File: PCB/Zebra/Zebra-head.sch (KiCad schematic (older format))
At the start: 4 parts, among them J1 Conn_01x11, J2 Conn_01x11, U1 ProMicro, U2 ssd1306

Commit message: Switch to foostan's footprint library, MIT license
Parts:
- removed U1: ProMicro, promicro:ProMicro-DualFootprint, symbol promicro:ProMicro
- added U1: ProMicro, kbd:ProMicro_v3.5, symbol kbd:ProMicro
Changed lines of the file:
@@
 Wire Wire Line
 	1750 3100 1450 3100
-$Comp
-L promicro:ProMicro U1
-U 1 1 5FCC9219
-P 2450 3250
-F 0 "U1" H 2450 4393 60  0000 C CNN
-F 1 "ProMicro" H 2450 4287 60  0000 C CNN
-F 2 "promicro:ProMicro-DualFootprint" H 2450 4181 60  0000 C CNN
-F 3 "" H 2550 2200 60  0000 C CNN
-	1    2450 3250
-	1    0    0    -1
-$EndComp
 Wire Wire Line
 	1650 2100 3800 2100
@@
 Wire Wire Line
 	950  2900 950  4950
+$Comp
+L kbd:ProMicro U1
+U 1 1 5FD08ED3
+P 2450 3050
+F 0 "U1" H 2450 3887 60  0000 C CNN
+F 1 "ProMicro" H 2450 3781 60  0000 C CNN
+F 2 "kbd:ProMicro_v3.5" H 2550 2000 60  0000 C CNN
+F 3 "" H 2550 2000 60  0000 C CNN
+	1    2450 3050
+	1    0    0    -1
+$EndComp
 $EndSCHEMATC

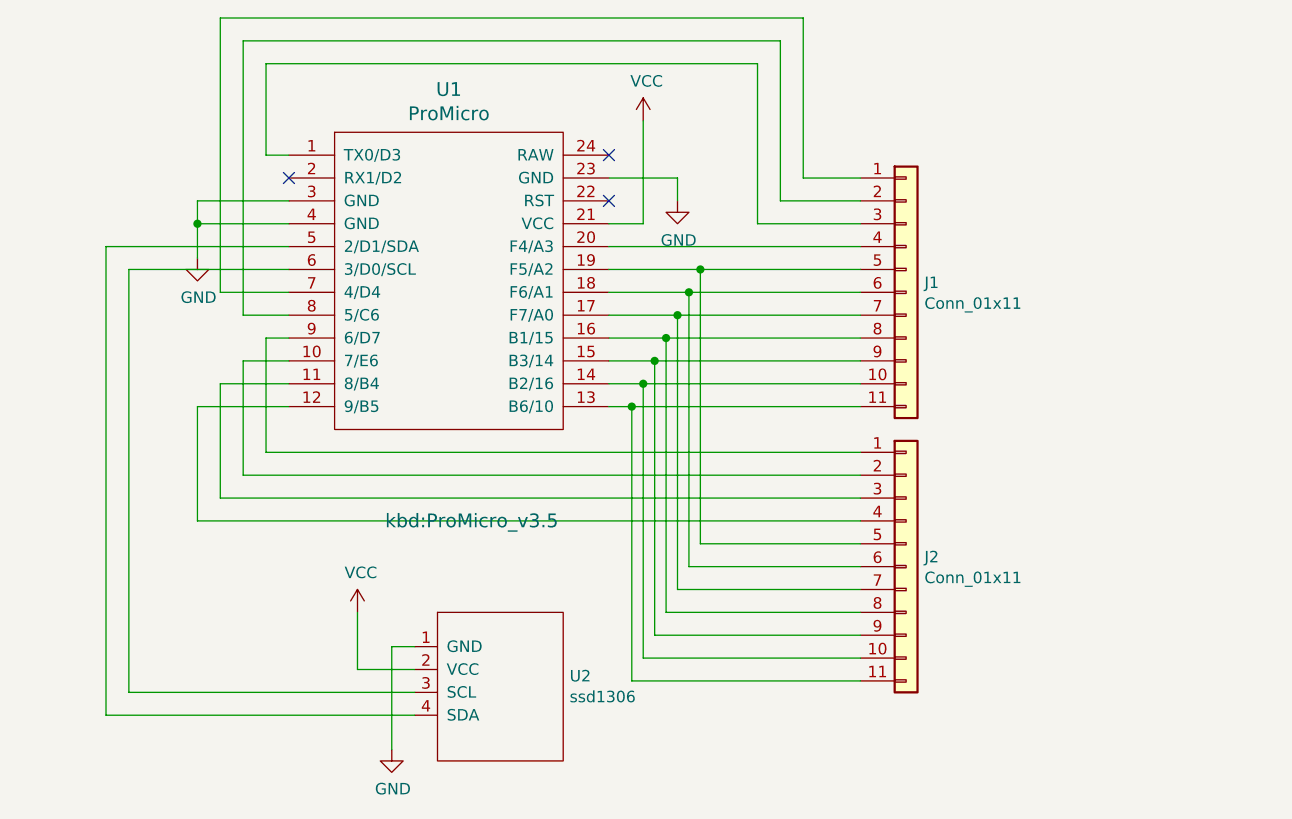
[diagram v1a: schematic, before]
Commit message: Add TRRS jack
With serial and optional I2C
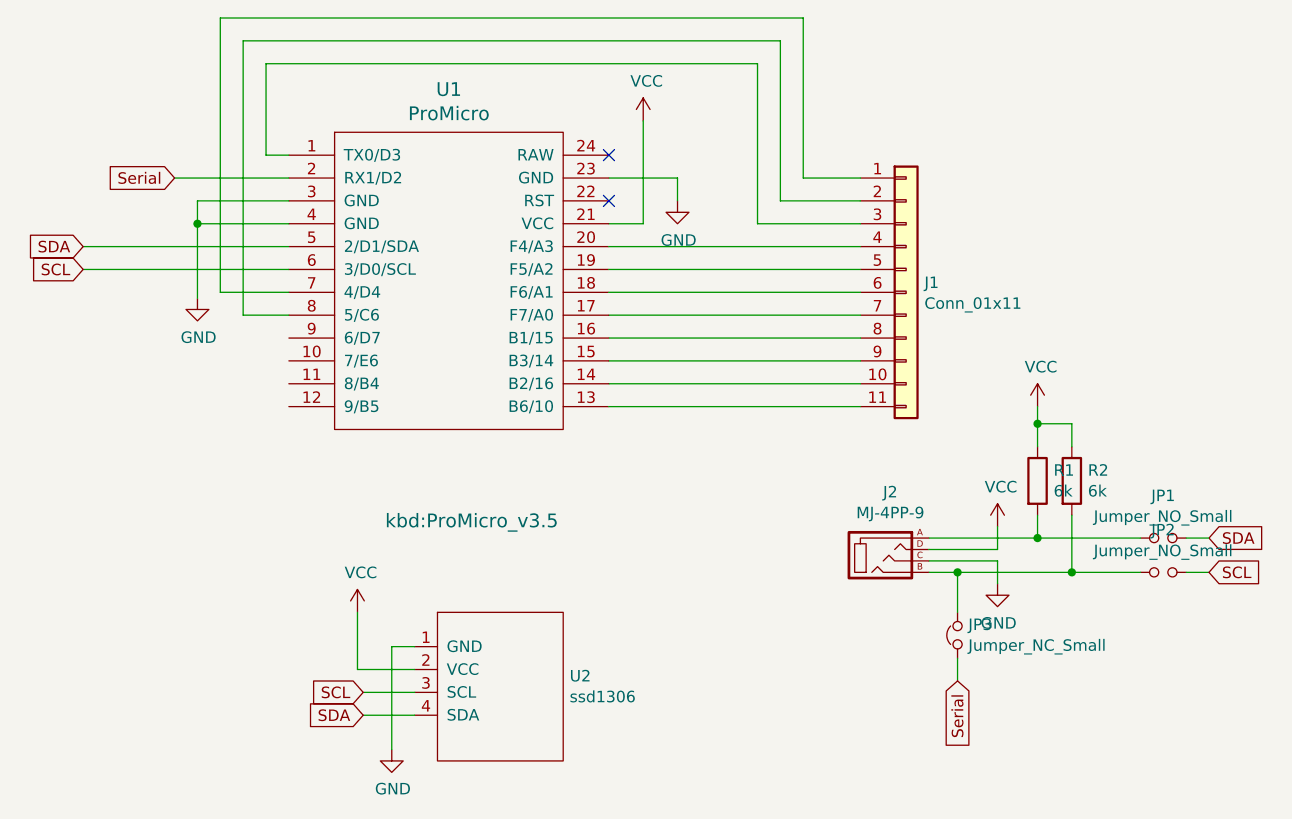
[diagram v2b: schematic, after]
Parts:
- removed J2: Conn_01x11, Connector_PinHeader_2.54mm:PinHeader_1x11_P2.54mm_Vertical, symbol Connector_Generic:Conn_01x11
- added J2: MJ-4PP-9, kbd:MJ-4PP-9_1side, symbol kbd:MJ-4PP-9
- added JP1, JP2: Jumper_NO_Small, Jumper:SolderJumper-2_P1.3mm_Open_Pad1.0x1.5mm, symbol Device:Jumper_NO_Small
- added JP3: Jumper_NC_Small, Jumper:SolderJumper-2_P1.3mm_Bridged_Pad1.0x1.5mm, symbol Device:Jumper_NC_Small
- added R1, R2: 6k, Resistor_SMD:R_1206_3216Metric_Pad1.30x1.75mm_HandSolder, symbol Device:R
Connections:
- net GND: now also J2.C
- net VCC: now also J2.D, R1.1, R2.1
- net SCL: now reaches U1.6 (3/D0/SCL), U2.3 (SCL)
- net SCL: now also JP2.2
- net SDA: now reaches U1.5 (2/D1/SDA), U2.4 (SDA)
- net SDA: now also JP1.2
- net Serial: now reaches U1.2 (RX1/D2)
- net Serial: now also JP3.1
- new net: J2.A, JP1.1, R1.2
- new net: J2.B, JP2.1, JP3.2, R2.2
- no-connect marks 3 -> 2
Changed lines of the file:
@@
 	1    0    0    -1
 $EndComp
-$Comp
-L Connector_Generic:Conn_01x11 J2
-U 1 1 5FA81425
-P 4450 4300
-F 0 "J2" H 4530 4342 50  0000 L CNN
-F 1 "Conn_01x11" H 4530 4251 50  0000 L CNN
-F 2 "Connector_PinHeader_2.54mm:PinHeader_1x11_P2.54mm_Vertical" H 4450 4300 50  0001 C CNN
-F 3 "~" H 4450 4300 50  0001 C CNN
-	1    4450 4300
-	1    0    0    -1
-$EndComp
-Wire Wire Line
-	4250 3600 3250 3600
-Wire Wire Line
-	3150 3500 3300 3500
-Wire Wire Line
-	4250 3400 3350 3400
-Wire Wire Line
-	3150 3300 3400 3300
-Wire Wire Line
-	4250 3200 3450 3200
-Wire Wire Line
-	3150 3100 3500 3100
-Wire Wire Line
-	4250 3000 3550 3000
-Wire Wire Line
-	3250 3600 3250 4800
-Wire Wire Line
-	3250 4800 4250 4800
-Connection ~ 3250 3600
-Wire Wire Line
-	3250 3600 3150 3600
-Wire Wire Line
-	3300 3500 3300 4700
-Wire Wire Line
-	3300 4700 4250 4700
-Connection ~ 3300 3500
-Wire Wire Line
-	3300 3500 4250 3500
-Wire Wire Line
-	3350 3400 3350 4600
-Wire Wire Line
-	3350 4600 4250 4600
-Connection ~ 3350 3400
-Wire Wire Line
-	3350 3400 3150 3400
-Wire Wire Line
-	3400 3300 3400 4500
-Wire Wire Line
-	3400 4500 4250 4500
-Connection ~ 3400 3300
-Wire Wire Line
-	3400 3300 4250 3300
-Wire Wire Line
-	3450 3200 3450 4400
-Wire Wire Line
-	3450 4400 4250 4400
-Connection ~ 3450 3200
-Wire Wire Line
-	3450 3200 3150 3200
-Wire Wire Line
-	3500 3100 3500 4300
-Wire Wire Line
-	3500 4300 4250 4300
-Connection ~ 3500 3100
-Wire Wire Line
-	3500 3100 4250 3100
-Wire Wire Line
-	3550 3000 3550 4200
-Wire Wire Line
-	3550 4200 4250 4200
-Connection ~ 3550 3000
-Wire Wire Line
-	3550 3000 3150 3000
 Wire Wire Line
 	3150 2900 4250 2900
 Wire Wire Line
-	1650 3800 4250 3800
-Wire Wire Line
-	1550 3900 4250 3900
-Wire Wire Line
-	1450 4000 4250 4000
-Wire Wire Line
-	1350 4100 4250 4100
-Wire Wire Line
 	1750 2500 1650 2500
 Wire Wire Line
@@
 Wire Wire Line
 	1750 2800 1350 2800
-Wire Wire Line
-	1350 2800 1350 2950
 $Comp
 L power:GND #PWR01
 U 1 1 5FAB7882
-P 1350 2950
-F 0 "#PWR01" H 1350 2700 50  0001 C CNN
-F 1 "GND" H 1355 2777 50  0000 C CNN
-F 2 "" H 1350 2950 50  0001 C CNN
-F 3 "" H 1350 2950 50  0001 C CNN
-	1    1350 2950
+P 1350 3125
+F 0 "#PWR01" H 1350 2875 50  0001 C CNN
+F 1 "GND" H 1355 2952 50  0000 C CNN
+F 2 "" H 1350 3125 50  0001 C CNN
+F 3 "" H 1350 3125 50  0001 C CNN
+	1    1350 3125
 	1    0    0    -1
 $EndComp
@@
 Wire Wire Line
 	3300 2800 3300 2350
-Wire Wire Line
-	1750 3000 1050 3000
-Wire Wire Line
-	1050 4850 2300 4850
-Wire Wire Line
-	1750 2900 950  2900
-Wire Wire Line
-	950  4950 2300 4950
 $Comp
 L power:GND #PWR03
@@
 NoConn ~ 3150 2500
 NoConn ~ 3150 2700
-NoConn ~ 1750 2600
-Wire Wire Line
-	1650 3300 1750 3300
-Wire Wire Line
-	1650 3300 1650 3800
-Wire Wire Line
-	1450 3500 1750 3500
-Wire Wire Line
-	1450 3500 1450 4000
-Wire Wire Line
-	1550 3400 1750 3400
-Wire Wire Line
-	1550 3400 1550 3900
-Wire Wire Line
-	1750 3600 1350 3600
-Wire Wire Line
-	1350 3600 1350 4100
 Wire Wire Line
 	1550 3200 1750 3200
@@
 	1650 2100 3800 2100
 Wire Wire Line
-	1050 3000 1050 4850
-Wire Wire Line
-	950  2900 950  4950
+	3150 3100 4250 3100
+Wire Wire Line
+	3150 3000 4250 3000
+Wire Wire Line
+	3150 3600 4250 3600
+Wire Wire Line
+	3150 3500 4250 3500
+Wire Wire Line
+	3150 3400 4250 3400
+Wire Wire Line
+	3150 3300 4250 3300
+Wire Wire Line
+	3150 3200 4250 3200
 $Comp
 L kbd:ProMicro U1
@@
 	1    0    0    -1
 $EndComp
+Text GLabel 1250 2600 0    50   Input ~ 0
+Serial
+Wire Wire Line
+	1750 2600 1250 2600
+$Comp
+L kbd:MJ-4PP-9 J2
+U 1 1 5FD0D110
+P 4350 4250
+F 0 "J2" H 4381 4526 50  0000 C CNN
+F 1 "MJ-4PP-9" H 4381 4435 50  0000 C CNN
+F 2 "kbd:MJ-4PP-9_1side" H 4625 4425 50  0001 C CNN
+F 3 "~" H 4625 4425 50  0001 C CNN
+	1    4350 4250
+	1    0    0    -1
+$EndComp
+$Comp
+L power:VCC #PWR0101
+U 1 1 5FD0DF7B
+P 4850 4125
+F 0 "#PWR0101" H 4850 3975 50  0001 C CNN
+F 1 "VCC" H 4865 4298 50  0000 C CNN
+F 2 "" H 4850 4125 50  0001 C CNN
+F 3 "" H 4850 4125 50  0001 C CNN
+	1    4850 4125
+	1    0    0    -1
+$EndComp
+Wire Wire Line
+	4550 4225 4850 4225
+$Comp
+L power:GND #PWR0102
+U 1 1 5FD10450
+P 4850 4375
+F 0 "#PWR0102" H 4850 4125 50  0001 C CNN
+F 1 "GND" H 4855 4202 50  0000 C CNN
+F 2 "" H 4850 4375 50  0001 C CNN
+F 3 "" H 4850 4375 50  0001 C CNN
+	1    4850 4375
+	1    0    0    -1
+$EndComp
+Wire Wire Line
+	4550 4275 4850 4275
+Text GLabel 4675 4800 3    50   Input ~ 0
+Serial
+Wire Wire Line
+	4550 4325 4675 4325
+$Comp
+L Device:Jumper_NO_Small JP1
+U 1 1 5FD0D318
+P 5575 4175
+F 0 "JP1" H 5575 4360 50  0000 C CNN
+F 1 "Jumper_NO_Small" H 5575 4269 50  0000 C CNN
+F 2 "Jumper:SolderJumper-2_P1.3mm_Open_Pad1.0x1.5mm" H 5575 4175 50  0001 C CNN
+F 3 "~" H 5575 4175 50  0001 C CNN
+	1    5575 4175
+	1    0    0    -1
+$EndComp
+$Comp
+L Device:Jumper_NO_Small JP2
+U 1 1 5FD0E0A1
+P 5575 4325
+F 0 "JP2" H 5575 4510 50  0000 C CNN
+F 1 "Jumper_NO_Small" H 5575 4419 50  0000 C CNN
+F 2 "Jumper:SolderJumper-2_P1.3mm_Open_Pad1.0x1.5mm" H 5575 4325 50  0001 C CNN
+F 3 "~" H 5575 4325 50  0001 C CNN
+	1    5575 4325
+	1    0    0    -1
+$EndComp
+Wire Wire Line
+	4850 4125 4850 4225
+Wire Wire Line
+	4850 4275 4850 4375
+Text GLabel 850  2900 0    50   Input ~ 0
+SDA
+Text GLabel 850  3000 0    50   Input ~ 0
+SCL
+Wire Wire Line
+	1750 2900 850  2900
+Wire Wire Line
+	1750 3000 850  3000
+Wire Wire Line
+	1350 2800 1350 3125
+Text GLabel 2075 4950 0    50   Input ~ 0
+SDA
+Text GLabel 2075 4850 0    50   Input ~ 0
+SCL
+Wire Wire Line
+	2300 4850 2075 4850
+Wire Wire Line
+	2300 4950 2075 4950
+Text GLabel 5775 4325 2    50   Input ~ 0
+SCL
+Text GLabel 5775 4175 2    50   Input ~ 0
+SDA
+$Comp
+L power:VCC #PWR0103
+U 1 1 5FD1F947
+P 5025 3600
+F 0 "#PWR0103" H 5025 3450 50  0001 C CNN
+F 1 "VCC" H 5040 3773 50  0000 C CNN
+F 2 "" H 5025 3600 50  0001 C CNN
+F 3 "" H 5025 3600 50  0001 C CNN
+	1    5025 3600
+	1    0    0    -1
+$EndComp
+$Comp
+L Device:R R1
+U 1 1 5FD1FE92
+P 5025 3925
+F 0 "R1" H 5095 3971 50  0000 L CNN
+F 1 "6k" H 5095 3880 50  0000 L CNN
+F 2 "Resistor_SMD:R_1206_3216Metric_Pad1.30x1.75mm_HandSolder" V 4955 3925 50  0001 C CNN
+F 3 "~" H 5025 3925 50  0001 C CNN
+	1    5025 3925
+	1    0    0    -1
+$EndComp
+$Comp
+L Device:R R2
+U 1 1 5FD2335A
+P 5175 3925
+F 0 "R2" H 5245 3971 50  0000 L CNN
+F 1 "6k" H 5245 3880 50  0000 L CNN
+F 2 "Resistor_SMD:R_1206_3216Metric_Pad1.30x1.75mm_HandSolder" V 5105 3925 50  0001 C CNN
+F 3 "~" H 5175 3925 50  0001 C CNN
+	1    5175 3925
+	1    0    0    -1
+$EndComp
+Wire Wire Line
+	5025 3775 5025 3675
+Wire Wire Line
+	5175 3775 5175 3675
+Wire Wire Line
+	5175 3675 5025 3675
+Connection ~ 5025 3675
+Wire Wire Line
+	5025 3675 5025 3600
+$Comp
+L Device:Jumper_NC_Small JP3
+U 1 1 5FD2C94B
+P 4675 4600
+F 0 "JP3" V 4721 4553 50  0000 R CNN
+F 1 "Jumper_NC_Small" V 4630 4553 50  0000 R CNN
+F 2 "Jumper:SolderJumper-2_P1.3mm_Bridged_Pad1.0x1.5mm" H 4675 4600 50  0001 C CNN
+F 3 "~" H 4675 4600 50  0001 C CNN
+	1    4675 4600
+	0    -1   -1   0
+$EndComp
+Wire Wire Line
+	4675 4325 4675 4500
+Wire Wire Line
+	4675 4700 4675 4800
+Wire Wire Line
+	5675 4175 5775 4175
+Wire Wire Line
+	5675 4325 5775 4325
+Connection ~ 4675 4325
+Wire Wire Line
+	4675 4325 5175 4325
+Wire Wire Line
+	4550 4175 5025 4175
+Wire Wire Line
+	5025 4075 5025 4175
+Connection ~ 5025 4175
+Wire Wire Line
+	5025 4175 5475 4175
+Wire Wire Line
+	5175 4075 5175 4325
+Connection ~ 5175 4325
+Wire Wire Line
+	5175 4325 5475 4325
 $EndSCHEMATC
